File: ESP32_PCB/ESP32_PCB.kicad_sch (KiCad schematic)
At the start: 22 parts, among them J1 USB_C_Receptacle, J2 ESC1, J3 ESC2, U1 ESP32-S3-MINI-1, U2 H3LIS331DL, U3 AP2112K-3.3

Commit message: start pcb
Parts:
- removed U1: ESP32-S3-MINI-1, PCM_Espressif:ESP32-S3-MINI-1, symbol PCM_Espressif:ESP32-S3-MINI-1
- added U5: ESP32-S3-MINI-1U, RF_Module:ESP32-S2-MINI-1U, symbol RF_Module:ESP32-S3-MINI-1U
- C5: footprint Capacitor_SMD:CP_Elec_3x5.3 -> Capacitor_Tantalum_SMD:CP_EIA-1608-08_AVX-J
- J2, J3: footprint (none) -> ESC_Connectors:3_Pin
- U2: footprint TFLGA16_3X3X1_STM -> accelerometer:TFLGA16_3X3X1_STM
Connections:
- net +3V3: now also U5.3 (3V3)
- net GNDREF: now also U5.1 (GND), U5.2 (GND), U5.42 (GND), U5.43 (GND), U5.46 (GND), U5.47 (GND), U5.48 (GND), U5.49 (GND), U5.50 (GND), U5.51 (GND), U5.52 (GND), U5.53 (GND), U5.54 (GND), U5.55 (GND), U5.56 (GND), U5.57 (GND), U5.58 (GND), U5.59 (GND), U5.60 (GND), U5.61 (GND), U5.62 (GND), U5.63 (GND), U5.64 (GND), U5.65 (GND)
- net S1: now also U5.6 (IO2)
- net S2: now also U5.8 (IO4)
- net SCL: now also U5.13 (IO9)
- net SDA: now also U5.12 (IO8)
- net at J1.A7 (D-), J1.B7 (D-): now also U5.23 (USB_D-)
- net at J1.A6 (D+), J1.B6 (D+): now also U5.24 (USB_D+)
- no-connect marks 39 -> 38
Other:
- moved on the sheet: C4

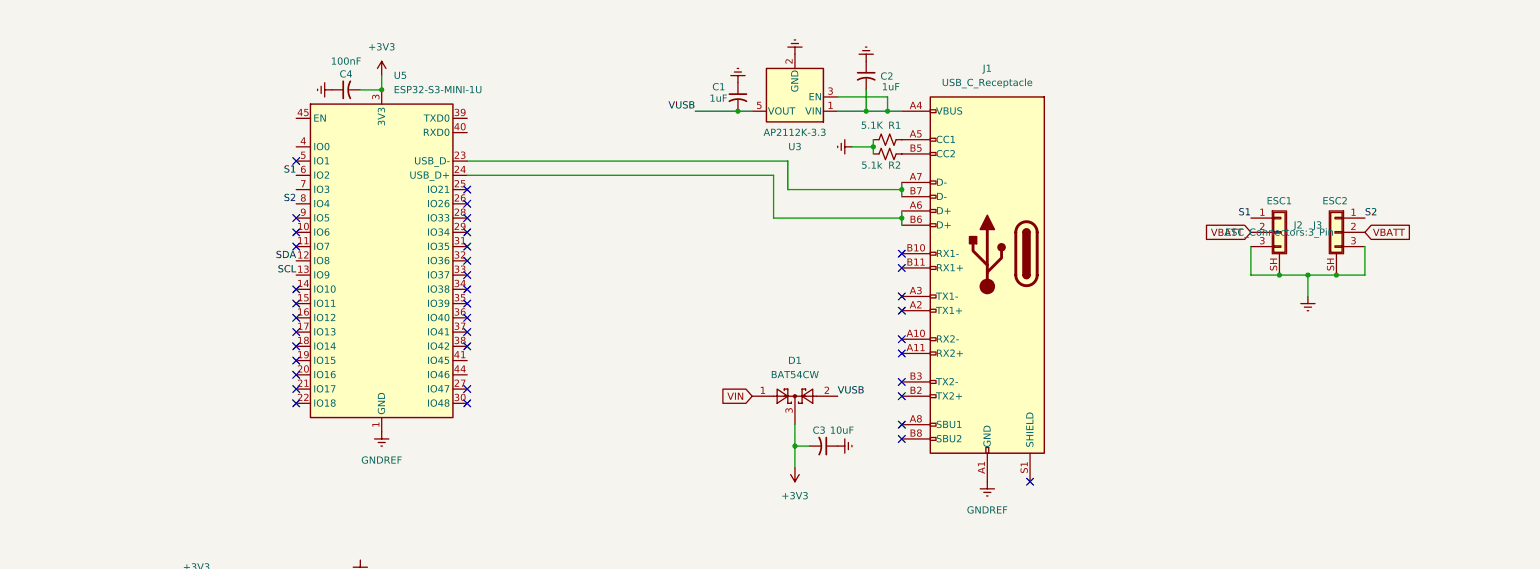
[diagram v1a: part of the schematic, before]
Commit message: fix pin assignments and add en and boot jumper
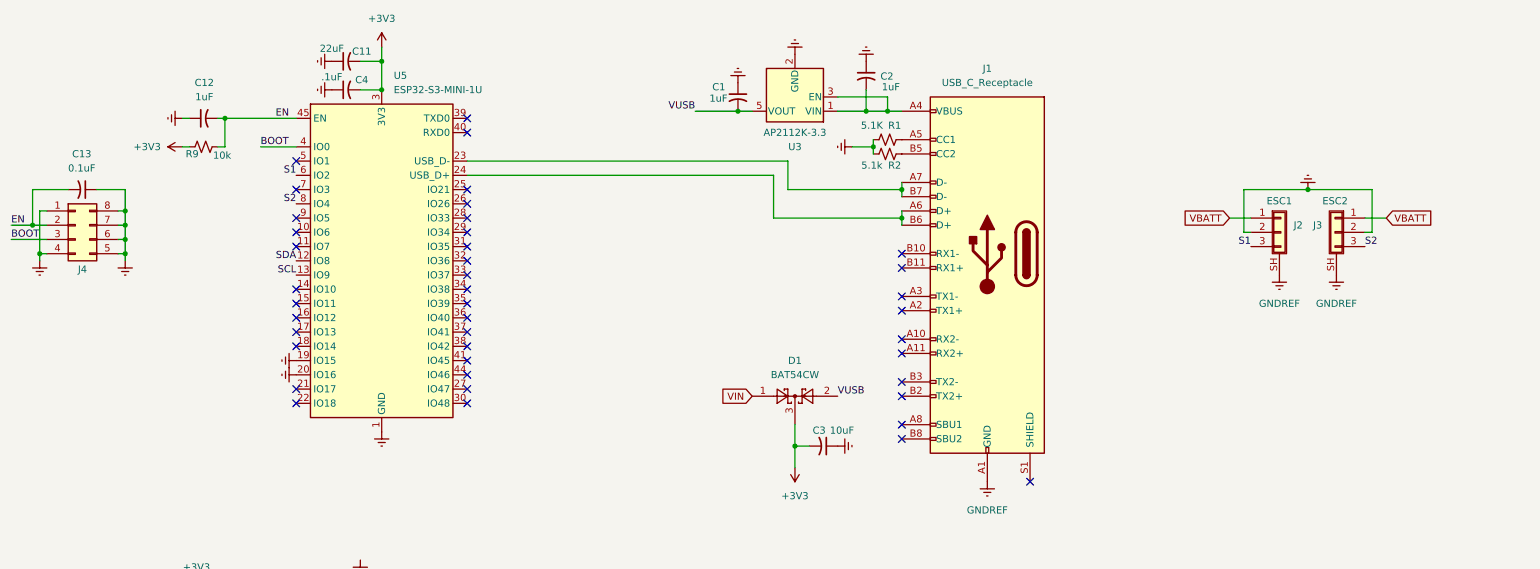
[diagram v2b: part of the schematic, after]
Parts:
- added C11: 22uF, Capacitor_SMD:C_0603_1608Metric, symbol Device:C_Small_US
- added C12: 1uF, Capacitor_SMD:C_0201_0603Metric, symbol Device:C_Small_US
- added C13: 0.1uF, Capacitor_SMD:C_0201_0603Metric, symbol Device:C_Small_US
- added J4: Conn_02x04_Counter_Clockwise, Connector_PinHeader_1.00mm:PinHeader_2x04_P1.00mm_Vertical, symbol Connector_Generic:Conn_02x04_Counter_Clockwise
- added R9: 10k, Resistor_SMD:R_0603_1608Metric, symbol Device:R_Small_US
- C4: value 100nF -> .1uF
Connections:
- net +3V3: now also C11.2, R9.2
- net GNDREF: now also J2.2 (Pin_2), J3.2 (Pin_2), U5.19 (IO15), U5.20 (IO16), C11.1, C12.1, C13.1, J4.1 (Pin_1), J4.4 (Pin_4), J4.5 (Pin_5), J4.6 (Pin_6), J4.7 (Pin_7), J4.8 (Pin_8); no longer J2.3 (Pin_3), J3.3 (Pin_3)
- net S1: now also J2.3 (Pin_3); no longer J2.1 (Pin_1)
- net S2: now also J3.3 (Pin_3); no longer J3.1 (Pin_1)
- net VBATT: now also J2.1 (Pin_1), J3.1 (Pin_1); no longer J2.2 (Pin_2), J3.2 (Pin_2)
- net BOOT: now reaches U5.4 (IO0)
- net BOOT: now also J4.3 (Pin_3)
- net EN: now reaches U5.45 (EN)
- net EN: now also C12.2, C13.2, J4.2 (Pin_2), R9.1
- no-connect marks 38 -> 41

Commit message: horizontal usb-c
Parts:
- J1: footprint Connector_USB:USB_C_Receptacle_GCT_USB4115-03-C -> Connector_USB:USB_C_Receptacle_Molex_105450-0101
- J4: footprint Connector_PinHeader_1.00mm:PinHeader_2x04_P1.00mm_Vertical -> Connector_PinSocket_1.00mm:PinSocket_2x04_P1.00mm_Vertical_SMD
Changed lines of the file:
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@@
 			)
 		)
-		(property "Footprint" "Connector_PinHeader_1.00mm:PinHeader_2x04_P1.00mm_Vertical"
+		(property "Footprint" "Connector_PinSocket_1.00mm:PinSocket_2x04_P1.00mm_Vertical_SMD"
 			(at 36.83 48.26 0)
 			(effects
@@
 			)
 		)
-		(property "Footprint" "Connector_USB:USB_C_Receptacle_GCT_USB4115-03-C"
+		(property "Footprint" "Connector_USB:USB_C_Receptacle_Molex_105450-0101"
 			(at 195.58 53.34 0)
 			(effects

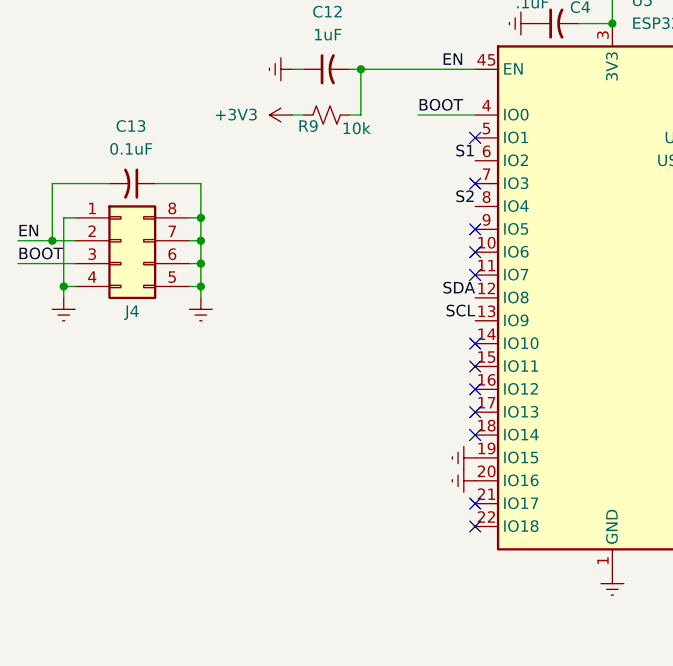
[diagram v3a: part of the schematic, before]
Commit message: Add LED pins, correct ESC signal pins
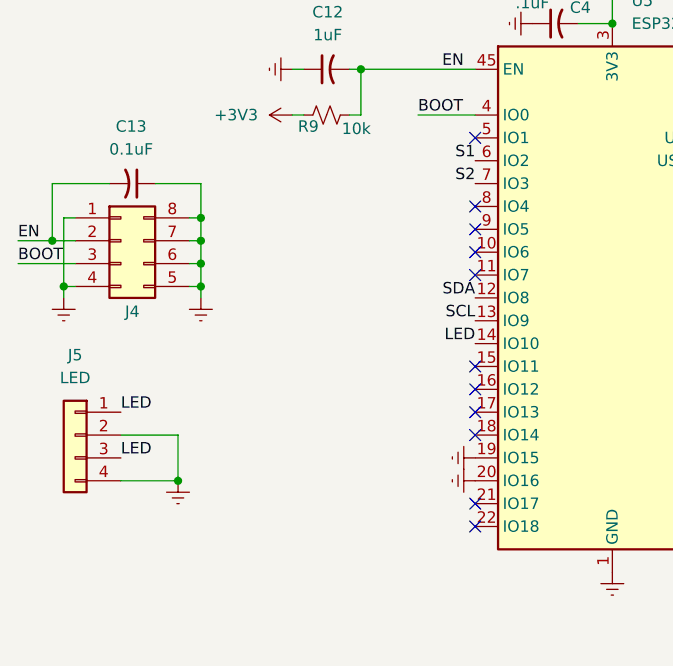
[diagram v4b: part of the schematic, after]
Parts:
- added J5: LED, ESC_Connectors:4_Pin, symbol Connector_Generic:Conn_01x04
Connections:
- net GNDREF: now also J5.2 (Pin_2), J5.4 (Pin_4)
- net S2: now also U5.7 (IO3); no longer U5.8 (IO4)
- net LED: now reaches U5.14 (IO10)
- net LED: now also J5.1 (Pin_1), J5.3 (Pin_3)
- no-connect marks 41 -> 40
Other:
- title: (none) -> Stuffed Crust ESP32_PCB
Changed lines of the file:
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@@
 	(generator_version "9.0")
 	(paper "A4")
+	(title_block
+		(title "Stuffed Crust ESP32_PCB")
+	)
 	(junction
 		(at 29.21 48.26)
@@
 	)
 	(junction
+		(at 43.18 74.93)
+		(diameter 0)
+		(color 0 0 0 0)
+	)
+	(junction
 		(at 132.08 128.27)
 		(diameter 0)
@@
 	)
 	(no_connect
-		(at 76.2 41.91)
-	)
-	(no_connect
 		(at 106.68 69.85)
 	)
@@
 	)
 	(no_connect
+		(at 76.2 44.45)
+	)
+	(no_connect
 		(at 106.68 29.21)
 	)
@@
 	)
 	(no_connect
-		(at 76.2 59.69)
-	)
-	(no_connect
 		(at 106.68 64.77)
 	)
@@
 	(wire
 		(pts
+			(xy 36.83 69.85) (xy 43.18 69.85)
+		)
+		(stroke
+			(width 0)
+			(type default)
+		)
+	)
+	(wire
+		(pts
 			(xy 129.54 115.57) (xy 129.54 123.19)
 		)
@@
 	(wire
 		(pts
+			(xy 36.83 74.93) (xy 43.18 74.93)
+		)
+		(stroke
+			(width 0)
+			(type default)
+		)
+	)
+	(wire
+		(pts
 			(xy 29.21 48.26) (xy 29.21 41.91)
 		)
@@
 	(wire
 		(pts
+			(xy 43.18 69.85) (xy 43.18 74.93)
+		)
+		(stroke
+			(width 0)
+			(type default)
+		)
+	)
+	(wire
+		(pts
 			(xy 179.07 34.29) (xy 179.07 35.56)
 		)
@@
 		)
 	)
+	(label "LED"
+		(at 36.83 72.39 0)
+		(effects
+			(font
+				(size 1.27 1.27)
+			)
+			(justify left bottom)
+		)
+	)
 	(label "EN"
 		(at 74.93 29.21 180)
@@
 		)
 	)
+	(label "SA0"
+		(at 90.17 152.4 0)
+		(effects
+			(font
+				(size 1.27 1.27)
+			)
+			(justify left bottom)
+		)
+	)
+	(label "LED"
+		(at 76.2 59.69 180)
+		(effects
+			(font
+				(size 1.27 1.27)
+			)
+			(justify right bottom)
+		)
+	)
 	(label "S2"
-		(at 76.2 44.45 180)
+		(at 76.2 41.91 180)
 		(effects
 			(font
@@
 		)
 	)
-	(label "SA0"
-		(at 90.17 152.4 0)
+	(label "LED"
+		(at 36.83 67.31 0)
 		(effects
 			(font
@@
 	)
 	(symbol
+		(lib_id "power:GNDREF")
+		(at 43.18 74.93 0)
+		(unit 1)
+		(exclude_from_sim no)
+		(in_bom yes)
+		(on_board yes)
+		(dnp no)
+		(fields_autoplaced yes)
+		(property "Reference" "#PWR036"
+			(at 43.18 81.28 0)
+			(effects
+				(font
+					(size 1.27 1.27)
+				)
+				(hide yes)
+			)
+		)
+		(property "Value" "GNDREF"
+			(at 43.18 80.01 0)
+			(effects
+				(font
+					(size 1.27 1.27)
+				)
+				(hide yes)
+			)
+		)
+		(property "Footprint" ""
+			(at 43.18 74.93 0)
+			(effects
+				(font
+					(size 1.27 1.27)
+				)
+				(hide yes)
+			)
+		)
+		(property "Datasheet" ""
+			(at 43.18 74.93 0)
+			(effects
+				(font
+					(size 1.27 1.27)
+				)
+				(hide yes)
+			)
+		)
+		(property "Description" "Power symbol creates a global label with name \"GNDREF\" , reference supply ground"
+			(at 43.18 74.93 0)
+			(effects
+				(font
+					(size 1.27 1.27)
+				)
+				(hide yes)
+			)
+		)
+		(pin "1"
+		)
+		(instances
+			(project "ESP32_PCB"
+				(path "/c820eee0-9a51-4601-b23c-3906ac354886"
+					(reference "#PWR036")
+					(unit 1)
+				)
+			)
+		)
+	)
+	(symbol
 		(lib_id "Device:R_Small_US")
 		(at 52.705 147.955 270)
@@
 					(unit 1)
 				)
+			)
+		)
+	)
+	(symbol
+		(lib_id "Connector_Generic:Conn_01x04")
+		(at 31.75 69.85 0)
+		(mirror y)
+		(unit 1)
+		(exclude_from_sim no)
+		(in_bom yes)
+		(on_board yes)
+		(dnp no)
+		(fields_autoplaced yes)
+		(property "Reference" "J5"
+			(at 31.75 60.96 0)
+			(effects
+				(font
+					(size 1.27 1.27)
+				)
+			)
+		)
+		(property "Value" "LED"
+			(at 31.75 63.5 0)
+			(effects
+				(font
+					(size 1.27 1.27)
+				)
+			)
+		)
+		(property "Footprint" "ESC_Connectors:4_Pin"
+			(at 31.75 69.85 0)
+			(effects
+				(font
+					(size 1.27 1.27)
+				)
+				(hide yes)
+			)
+		)
+		(property "Datasheet" "~"
+			(at 31.75 69.85 0)
+			(effects
+				(font
+					(size 1.27 1.27)
+				)
+				(hide yes)
+			)
+		)
+		(property "Description" "Generic connector, single row, 01x04, script generated (kicad-library-utils/schlib/autogen/connector/)"
+			(at 31.75 69.85 0)
+			(effects
+				(font
+					(size 1.27 1.27)
+				)
+				(hide yes)
+			)
+		)
+		(pin "4"
+		)
+		(pin "3"
+		)
+		(pin "1"
+		)
+		(pin "2"
+		)
+		(instances
+			(project ""
+				(path "/c820eee0-9a51-4601-b23c-3906ac354886"
+					(reference "J5")
+					(unit 1)
+				)

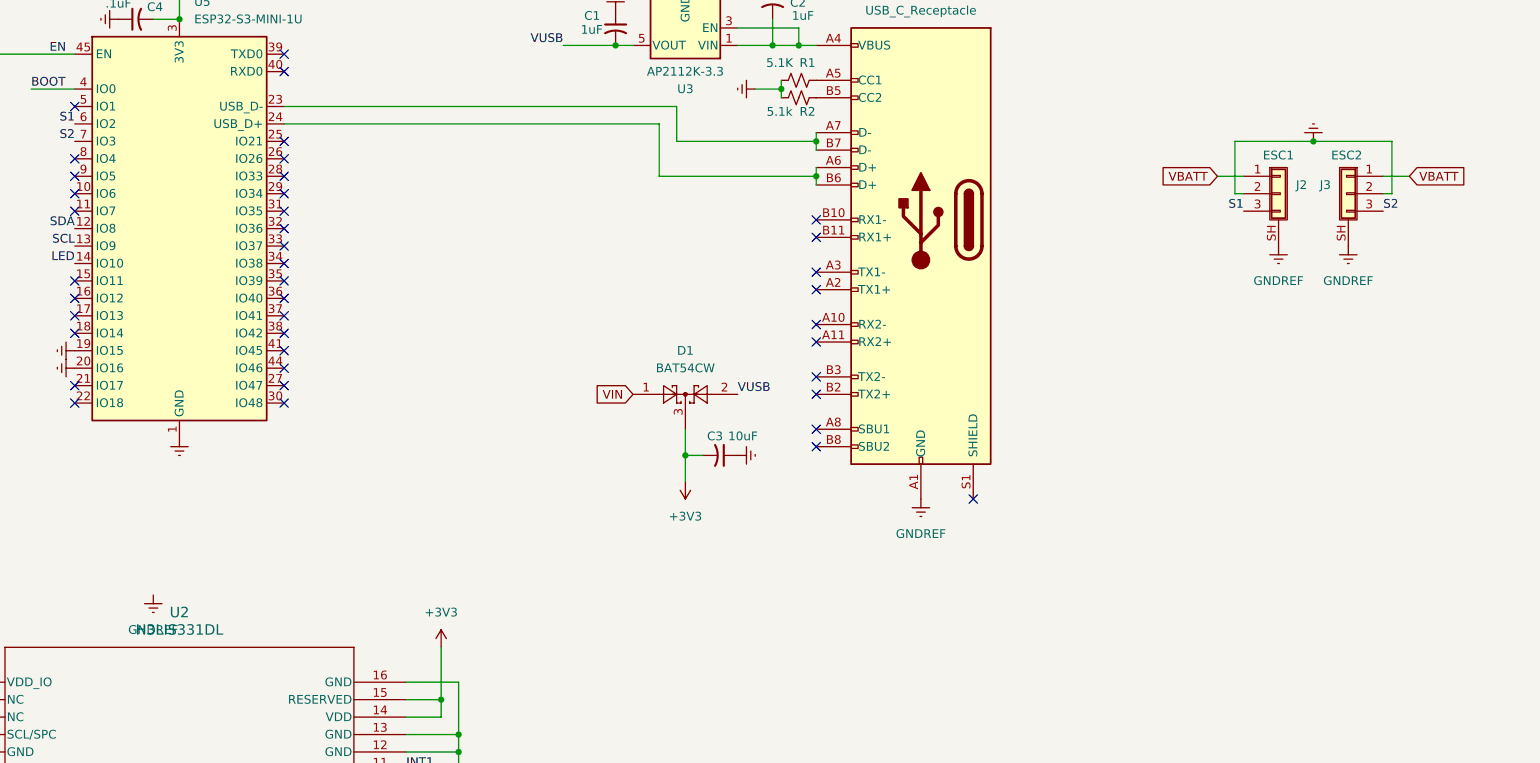
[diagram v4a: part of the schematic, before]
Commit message: Add two diodes for VBATT pins
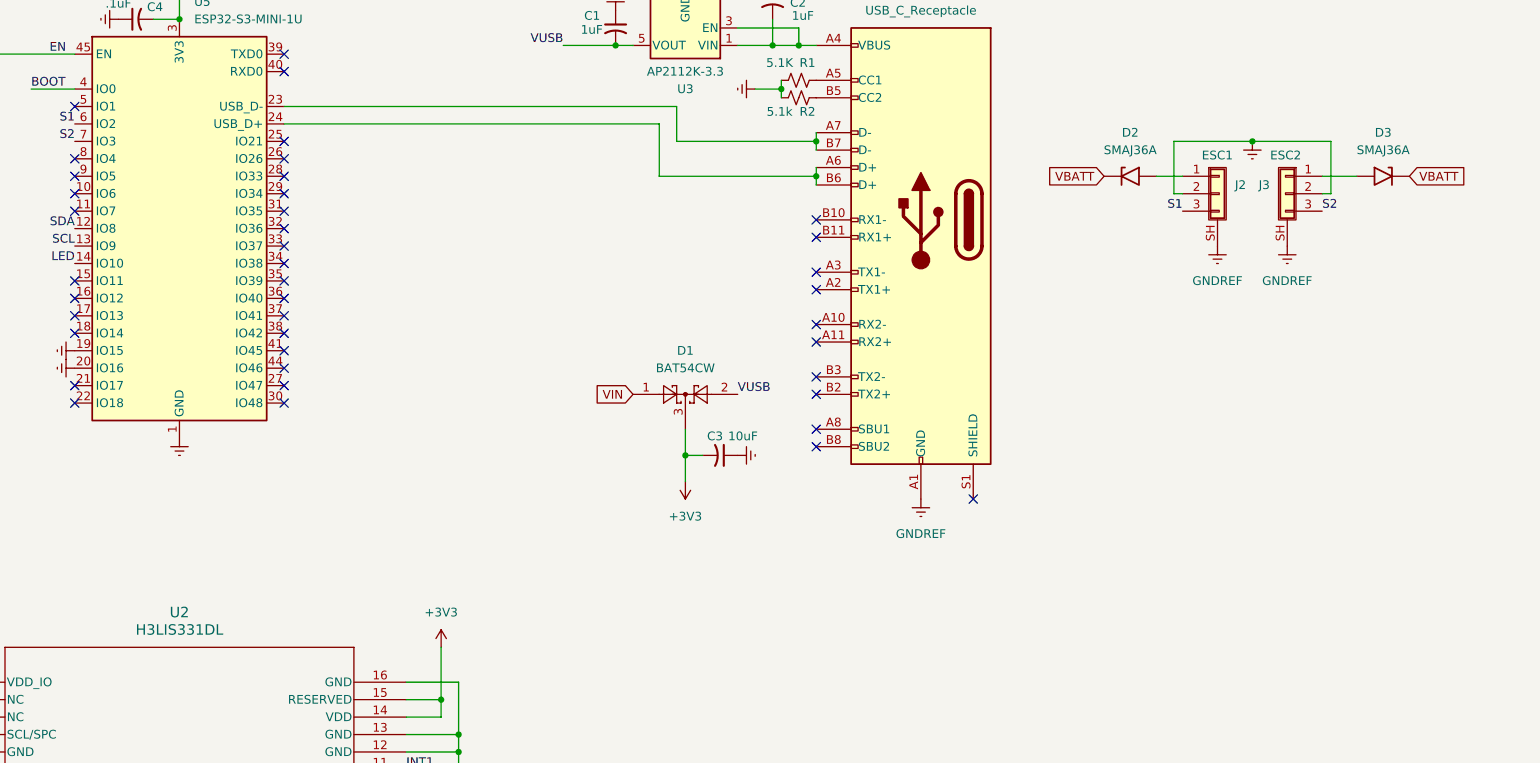
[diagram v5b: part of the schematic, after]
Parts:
- added D2, D3: SMAJ36A, Diode_SMD:D_SMA, symbol Diode:SMAJ36A
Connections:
- net VBATT: now also D2.1 (A1), D3.1 (A1); no longer J2.1 (Pin_1), J3.1 (Pin_1)
- new net: D3.2 (A2), J3.1 (Pin_1)
- new net: D2.2 (A2), J2.1 (Pin_1)
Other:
- moved on the sheet: J2, J3

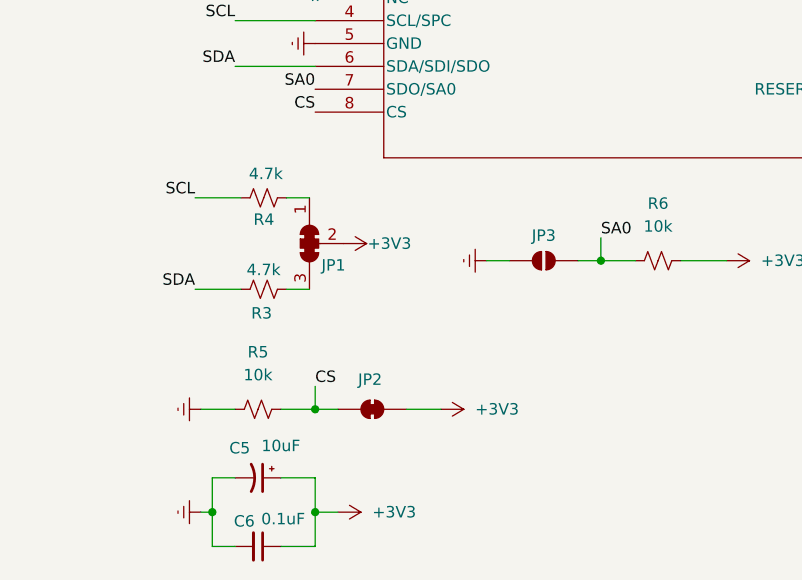
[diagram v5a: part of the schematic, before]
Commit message: Replace jumpers on the gyro with direct wires to avoid soldering issue
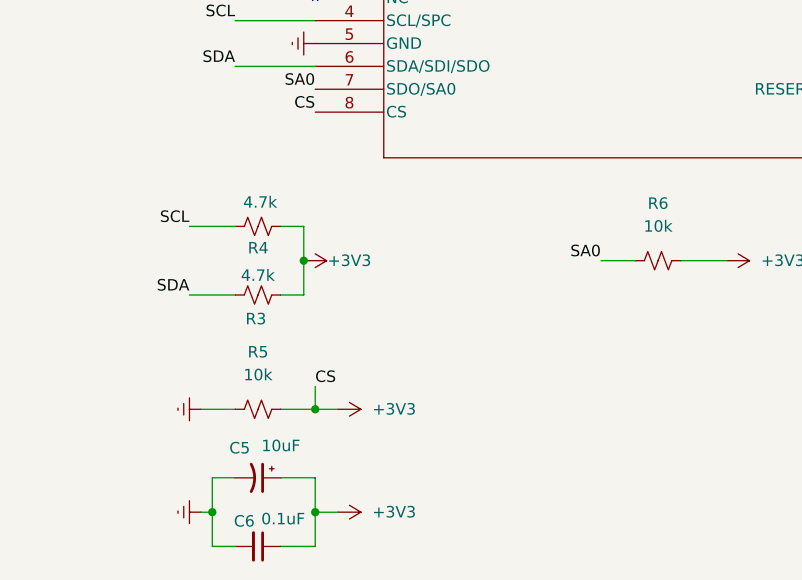
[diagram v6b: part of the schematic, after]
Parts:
- removed JP1: SolderJumper_3_Bridged123, Jumper:SolderJumper-3_P1.3mm_Bridged123_RoundedPad1.0x1.5mm, symbol Jumper:SolderJumper_3_Bridged123
- removed JP2: SolderJumper_2_Bridged, Jumper:SolderJumper-2_P1.3mm_Bridged_Pad1.0x1.5mm, symbol Jumper:SolderJumper_2_Bridged
- removed JP3: SolderJumper_2_Open, Jumper:SolderJumper-2_P1.3mm_Open_RoundedPad1.0x1.5mm, symbol Jumper:SolderJumper_2_Open
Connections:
- net CS is gone; now on net +3V3: R5.2, U2.8 (CS)
- net +3V3: now also R3.1, R4.1
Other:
- moved on the sheet: R3, R4
